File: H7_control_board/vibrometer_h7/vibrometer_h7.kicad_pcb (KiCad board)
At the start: 4 copper layers, 69.5 x 69.5 mm, 193 parts, among them J201 Conn_01x04_Socket, J202 Conn_02x06, J204 TC2030-NL, J301 USB_C_Receptacle_USB2.0_16P, J501 Conn_02x08_Odd_Even, J502 Conn_02x08_Odd_Even, J601 Conn_01x08_Socket, J701 Conn_01x08_Socket, J801 Conn_01x08_Socket, J901 PJ-3270, Q201 BSS138, Q202 BSS138, Q203 BSS138, SW201 SW_Push, SW501 SW_Push, SW502 SW_Push, U201 STM32H723VGTx, U301 USBLC6-2SC6, U302 MT9700, U303 AMS1117-3V3, U901 RC4580, U902 TPA6111A2, Y201 24MHz

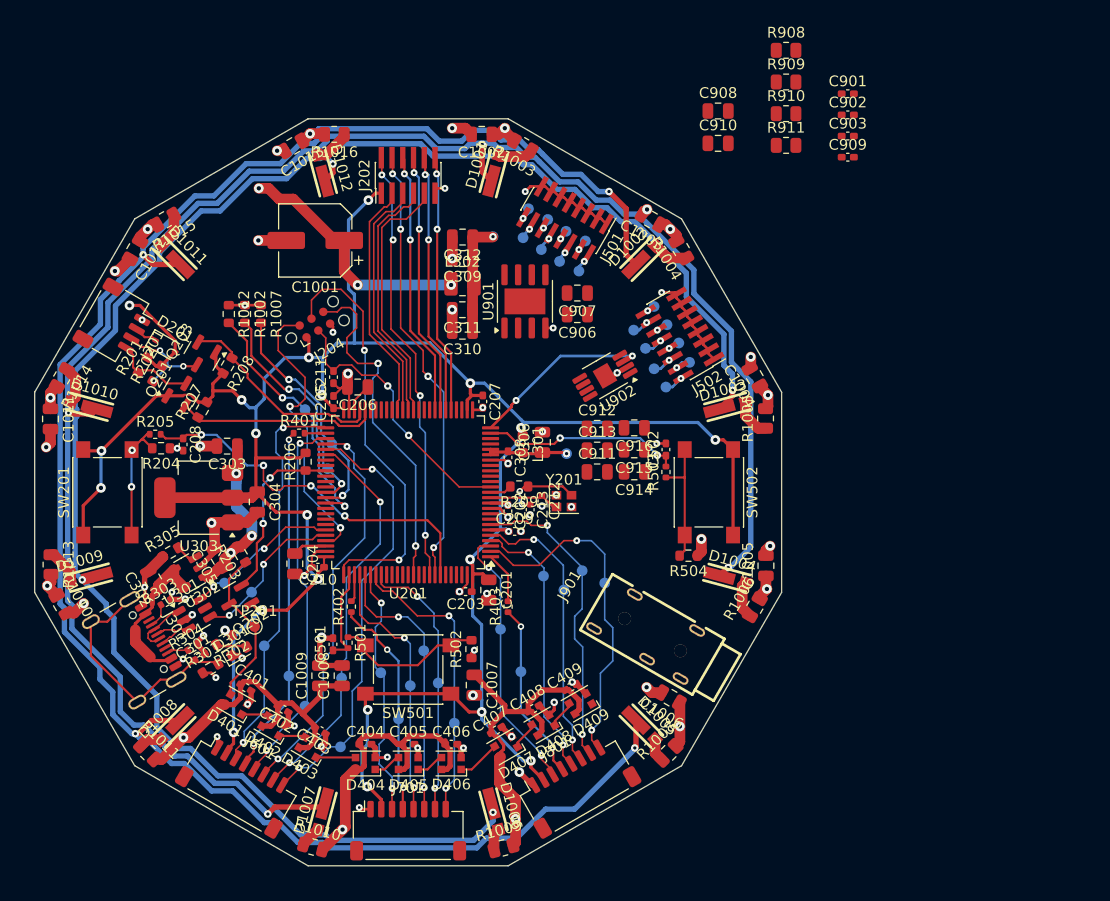
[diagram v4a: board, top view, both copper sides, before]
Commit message: zero unrouts! But still need to fix footprint for headphone jack. So 3 unrouts!
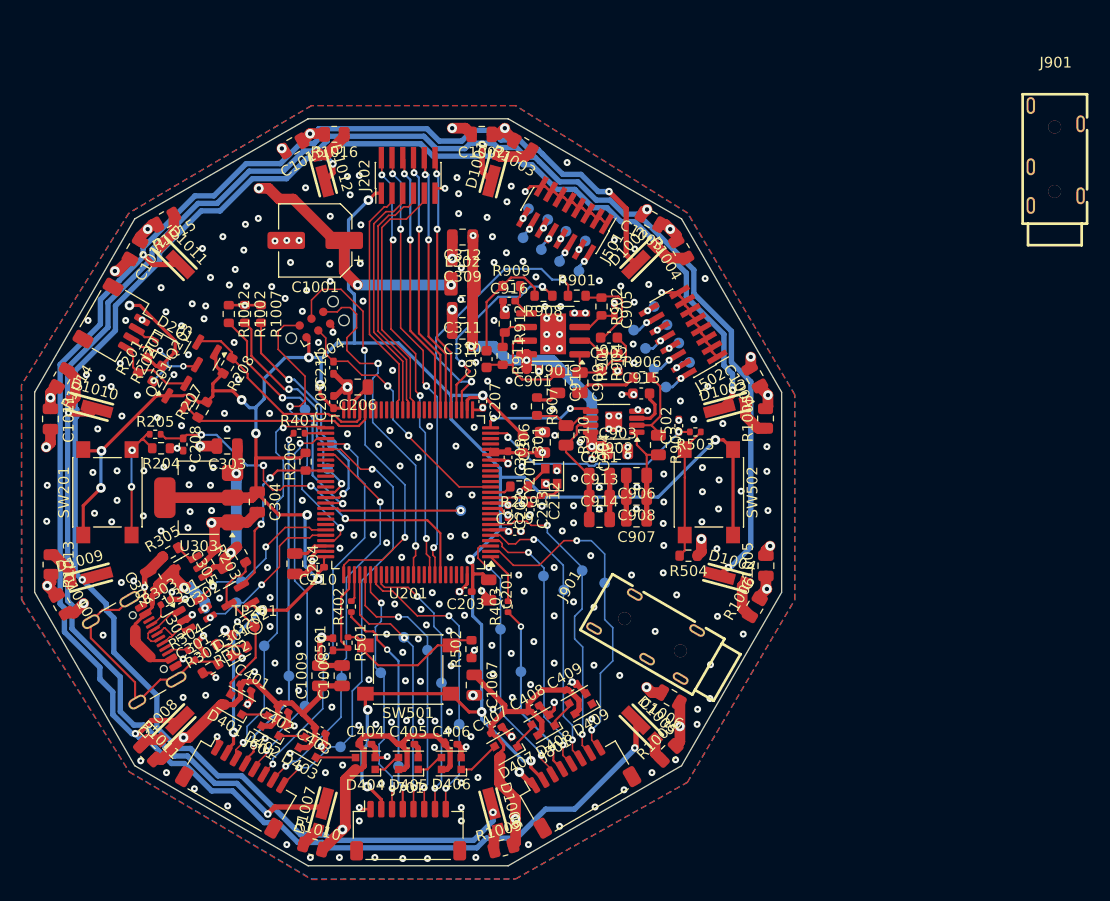
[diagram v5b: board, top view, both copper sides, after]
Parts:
- added C902: C_Small, Capacitor_SMD:C_0603_1608Metric, F.Cu at (168.7, 85.6)
- added C912: C_Small, Capacitor_SMD:C_0603_1608Metric, F.Cu at (157.3, 87.6)
- added J901: PJ-3270, footprints:AUDIO-TH_PJ-3270, F.Cu at (210.3, 68.6)
- added R901: R_Small_US, Resistor_SMD:R_0603_1608Metric, F.Cu at (165.7, 81.7)
- added R902: R_Small_US, Resistor_SMD:R_0603_1608Metric, F.Cu at (168.0, 82.7)
- added R904: R_Small_US, Resistor_SMD:R_0603_1608Metric, F.Cu at (168.0, 87.9)
- added R905: R_Small_US, Resistor_SMD:R_0603_1608Metric, F.Cu at (169.5, 87.9)
- added R908: R_Small_US, Resistor_SMD:R_0603_1608Metric, F.Cu at (162.6, 81.7)
- added R909: R_Small_US, Resistor_SMD:R_0603_1608Metric, F.Cu at (159.6, 80.8)
- added R911: R_Small_US, Resistor_SMD:R_0603_1608Metric, F.Cu at (158.8, 87.3)
- added R912: R_Small_US, Resistor_SMD:R_0603_1608Metric, F.Cu at (159.0, 84.3)
- added TP202: DAC TRG, TestPoint:TestPoint_Pad_D1.0mm, B.Cu at (154.9, 101.7)
- C915: renamed from C910; footprint Capacitor_SMD:C_0805_2012Metric -> Capacitor_SMD:C_0603_1608Metric
- R906: renamed from R908; footprint Resistor_SMD:R_0805_2012Metric -> Resistor_SMD:R_0603_1608Metric
- R907: renamed from R909; footprint Resistor_SMD:R_0805_2012Metric -> Resistor_SMD:R_0603_1608Metric
- moved C901 38.9 mm to (161.6, 88.5), turned to 180 degrees
- moved R907 38.1 mm to (162.0, 92.0), turned to -90 degrees
- moved C904 36.4 mm to (167.1, 96.3), turned to -90 degrees
- moved C916 35.1 mm to (159.4, 82.2)
- moved R910 33.9 mm to (164.7, 94.7), turned to -90 degrees
- moved R906 33.3 mm to (171.8, 89.3)
- moved R903 33.1 mm to (173.3, 95.6), turned to -90 degrees
- moved C903 33.1 mm to (169.5, 96.2)
- moved C905 28.3 mm to (169.2, 83.0), turned to -90 degrees
- moved C915 24.4 mm to (171.7, 90.8)
- moved C907 9.19 mm to (171.3, 102.5), turned to 180 degrees
- moved C914 9.12 mm to (167.8, 102.5), turned to 0 degrees
- moved C910 8.55 mm to (163.9, 89.8), turned to -90 degrees
- moved C909 6.34 mm to (166.0, 89.8), turned to -90 degrees
- moved C908 5.72 mm to (171.3, 100.5), turned to 180 degrees
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- renumbered C908 to C903, C909 to C904, C902 to C905, C911 to C906, C912 to C907, C913 to C908, C906 to C909, C907 to C910, C914 to C911, C915 to C913, C916 to C914, C903 to C916, R910 to R903, R911 to R910
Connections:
- U902 pad 1: /AUDIO/LN_BYPASS -> /AUDIO/LN_OUT1
- U902 pad 2: GND -> /AUDIO/LN_IN1
- U902 pad 3: /AUDIO/MUTE_SIGNAL -> /AUDIO/LN_BYPASS
- U902 pad 4: /AUDIO/LN_IN2 -> GND
- U902 pad 5: /AUDIO/LN_OUT2 -> /AUDIO/MUTE_SIGNAL
- U902 pad 6: +5VA -> /AUDIO/LN_IN2
- U902 pad 7: /AUDIO/LN_OUT1 -> /AUDIO/LN_OUT2
- U902 pad 8: /AUDIO/LN_IN1 -> +5VA
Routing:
- net /AUDIO/DAC_OUTA: track 0.00 -> 25.6 mm, vias 0 -> 2
- net +5VA: track 10.8 -> 33.5 mm, vias 1 -> 5
- net /AUDIO/DAC_OUTB: track 0.00 -> 18.9 mm, vias 0 -> 2
- net /MCU/DAC_EXT_TRG: track 0.00 -> 12.7 mm, vias 0 -> 1
- net /AUDIO/AMP2_FILT: track 0.00 -> 11.3 mm
- net /AUDIO/LN_OUT2: track 0.00 -> 11.3 mm
- net /AUDIO/AMP2_OUT: track 0.00 -> 11.2 mm
- net +3V3: track 255.4 -> 265.3 mm, vias 22 -> 21
- net /AUDIO/LN_OUT1: track 0.00 -> 9.54 mm
- net /AUDIO/AMP1_OUT: track 0.00 -> 8.84 mm
- net /AUDIO/AMP1_FILT: track 0.00 -> 8.10 mm
- net /AUDIO/LN_IN1: track 0.00 -> 7.71 mm
- net /AUDIO/MUTE_SIGNAL: track 17.1 -> 10.5 mm
- net /AUDIO/LN_IN2: track 0.00 -> 5.71 mm
- net Net-(C909-Pad2): track 0.00 -> 5.58 mm
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- added copper zone on B.Cu, net GND
- added copper zone on F.Cu, net GND

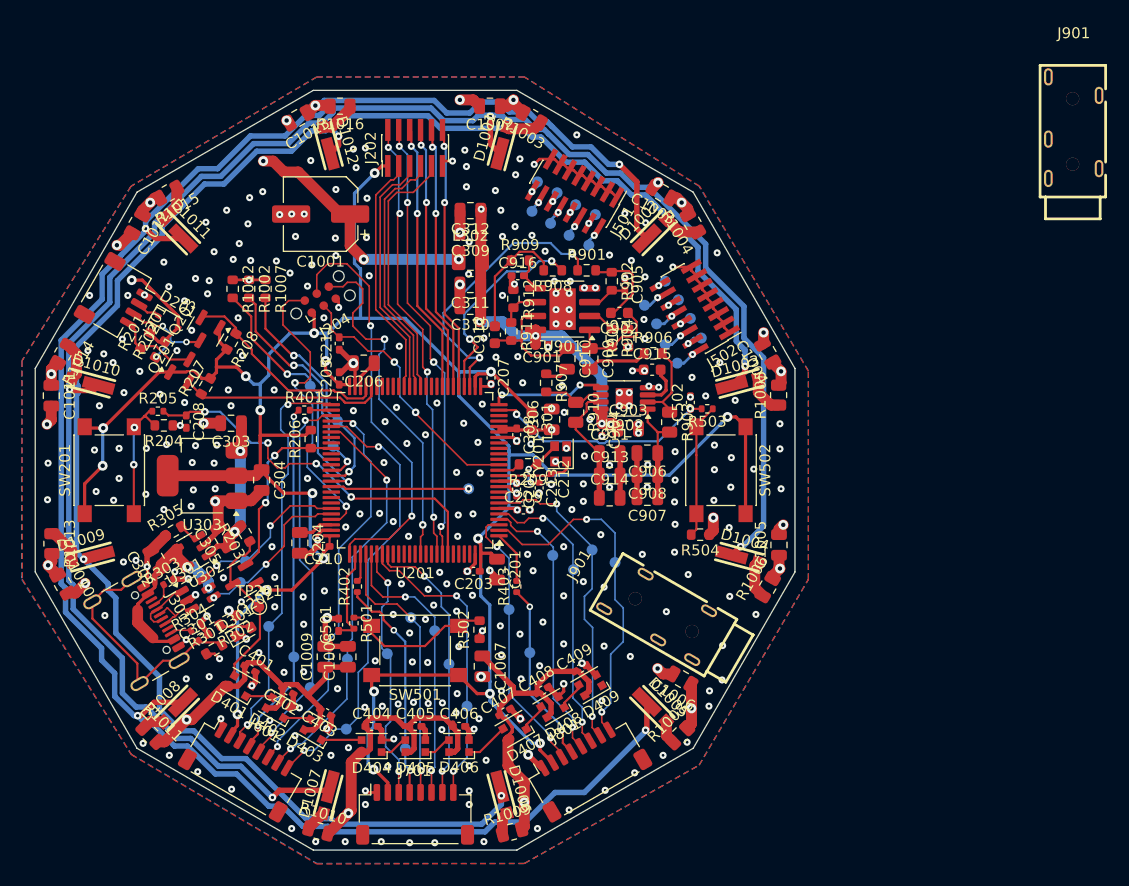
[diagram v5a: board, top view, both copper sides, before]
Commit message: cleaned up silkscreen
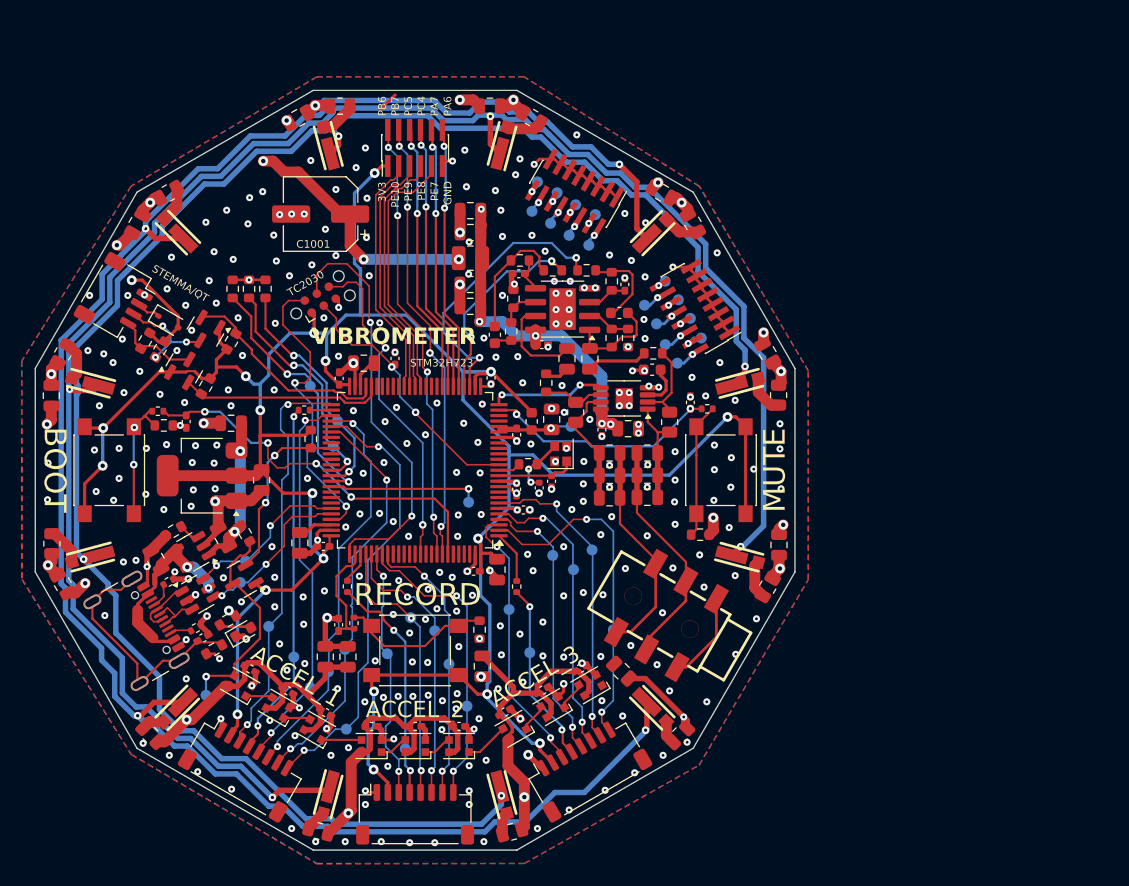
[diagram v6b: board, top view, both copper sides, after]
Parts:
- removed the J901 at (210.3, 68.6)
- removed the J901 at (172.5, 113.0)
- added J901: PH-313D, footprints:AUDIO-SMD_PJ-313D-2, F.Cu at (173.0, 113.3)
- TP201: moved to B.Cu
- moved TP201 9.44 mm to (130.9, 120.6), turned to 180 degrees
- moved TP414 6.16 mm to (168.2, 114.6)
- moved C1006 5.57 mm to (168.9, 118.4), turned to 135 degrees
- moved C211 5.29 mm to (148.2, 89.8), turned to -90 degrees
- moved TP304 1.80 mm to (164.3, 96.0)
- moved TP305 1.45 mm to (156.1, 77.5)
- moved TP202 1.23 mm to (154.9, 102.9)
- moved TP405 0.92 mm to (143.6, 116.4)
- moved R402 0.91 mm to (143.8, 110.6)
- moved TP407 0.45 mm to (142.1, 118.5)
- moved C212 0.21 mm to (162.5, 101.0)
- moved C916 0.20 mm to (159.5, 82.0)
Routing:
- net /AUDIO/AUDIO_R: track 4.05 -> 21.3 mm
- net /AUDIO/AUDIO_L: track 4.10 -> 20.0 mm
- net +5V: track 184.1 -> 188.6 mm
- net /ACCEL/LED_ACCEL: track 15.6 -> 19.9 mm, vias 0 -> 1
- net GND: track 120.7 -> 125.0 mm, vias 329 -> 327
- net (no net): track 0.00 -> 1.96 mm
- net +3V3A: track 5.85 -> 7.74 mm
- net /MCU/SWD_SWO: track 32.3 -> 30.6 mm
- net /MCU/BIG_RED_BUTTON: track 8.89 -> 10.4 mm
- net /MCU/DAC_EXT_TRG: track 12.7 -> 13.9 mm
- net +5VA: track 33.5 -> 34.7 mm
- net /ACCEL/ACCEL.INTA3: track 32.1 -> 31.3 mm
- net /ACCEL/SPI ACCELEROMETER2/ACCEL_SCK: track 20.8 -> 21.4 mm
- net +3V3: track 265.3 -> 264.7 mm
- net /ACCEL/ACCEL.INTB3: track 29.0 -> 28.4 mm
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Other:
- board text added: "3V3"
- board text added: "ACCEL_1"
- board text added: "ACCEL_2"
- board text added: "ACCEL_3"
- board text added: "BOOT"
- board text added: "GND"
- board text added: "MUTE"
- board text added: "PA6"
- board text added: "PA7"
- board text added: "PB6"
- board text added: "PB7"
- board text added: "PC4"
- board text added: "PC5"
- board text added: "PE10"
- board text added: "PE7"
- board text added: "PE8"
- board text added: "PE9"
- board text added: "RECORD"
- board text added: "STEMMA/QT"
- board text added: "STM32H723"
- board text added: "TC2030"
- board text added: "VIBROMETER"

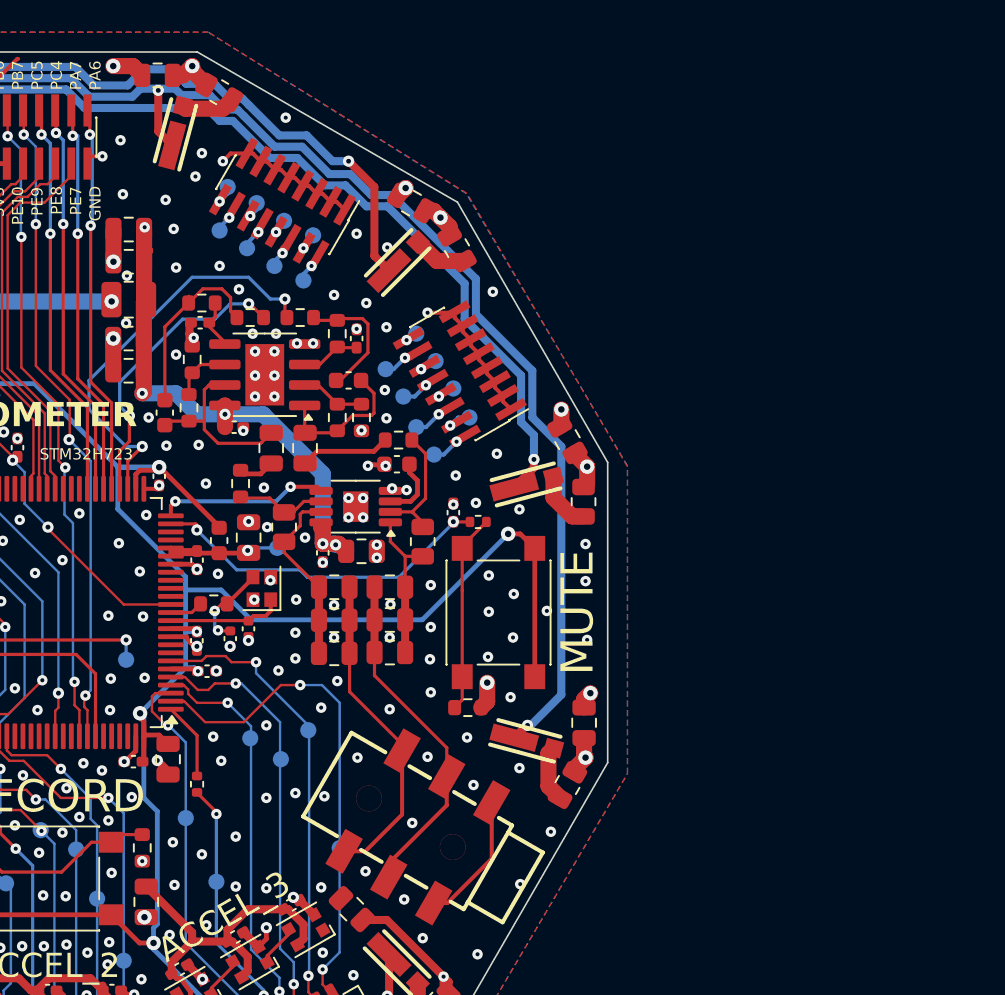
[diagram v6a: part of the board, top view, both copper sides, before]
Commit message: added indicator leds
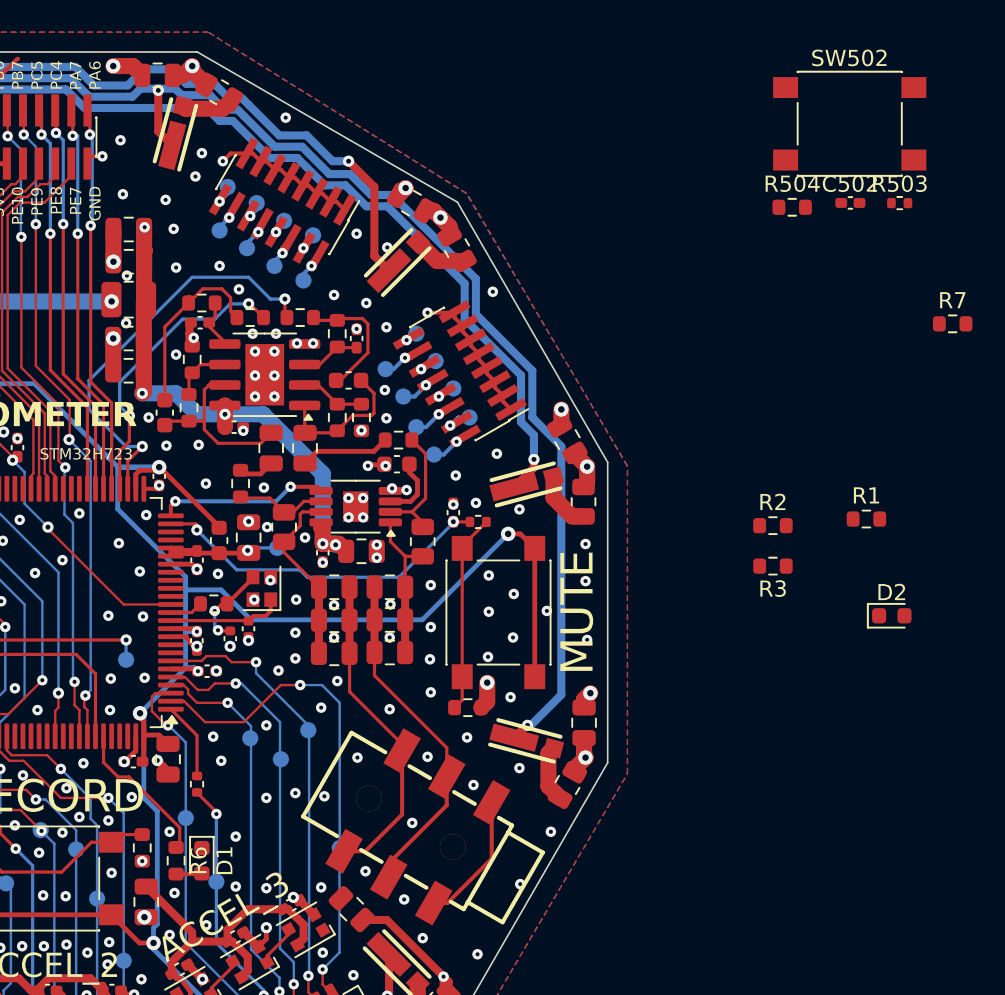
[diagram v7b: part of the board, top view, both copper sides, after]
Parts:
- added C502: 100n, Capacitor_SMD:C_0402_1005Metric_Pad0.74x0.62mm_HandSolder, F.Cu at (199.8, 74.6)
- added D1: LED, LED_SMD:LED_0603_1608Metric, F.Cu at (159.6, 115.4)
- added D2: LED, LED_SMD:LED_0603_1608Metric, F.Cu at (202.4, 100.2)
- added R1: 0, Resistor_SMD:R_0603_1608Metric, F.Cu at (200.8, 94.2)
- added R2: 0, Resistor_SMD:R_0603_1608Metric, F.Cu at (195.0, 94.6)
- added R3: 0, Resistor_SMD:R_0603_1608Metric, F.Cu at (195.0, 97.1)
- added R503: 330, Resistor_SMD:R_0402_1005Metric, F.Cu at (202.9, 74.6)
- added R504: 10k, Resistor_SMD:R_0603_1608Metric, F.Cu at (196.2, 74.9)
- added R6: 1k, Resistor_SMD:R_0603_1608Metric, F.Cu at (158.0, 115.4)
- added R7: 1k, Resistor_SMD:R_0603_1608Metric, F.Cu at (206.2, 82.1)
- added SW502: SW_Push, Button_Switch_SMD:SW_SPST_PTS645, F.Cu at (199.8, 69.7)
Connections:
- U201 pad 23: unconnected-(U201-PA1-Pad23) -> /MCU/MUTE_INDICATOR
- U201 pad 95: unconnected-(U201-PB8-Pad95) -> /MCU/RECORD_INDICATOR
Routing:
- net /MCU/RECORD_INDICATOR: track 0.00 -> 9.35 mm
- net Net-(D1-A): track 0.00 -> 1.62 mm
- net GND: vias 327 -> 325
